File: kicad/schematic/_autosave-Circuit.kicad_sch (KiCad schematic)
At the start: 54 parts, among them M1 Motor_DC, M2 Motor_DC, M3 Motor_DC, M4 Motor_DC, M5 Motor_DC, M6 Motor_DC, M7 Motor_DC, M8 Motor_DC, Q1 AO3400A, Q2 AO3400A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

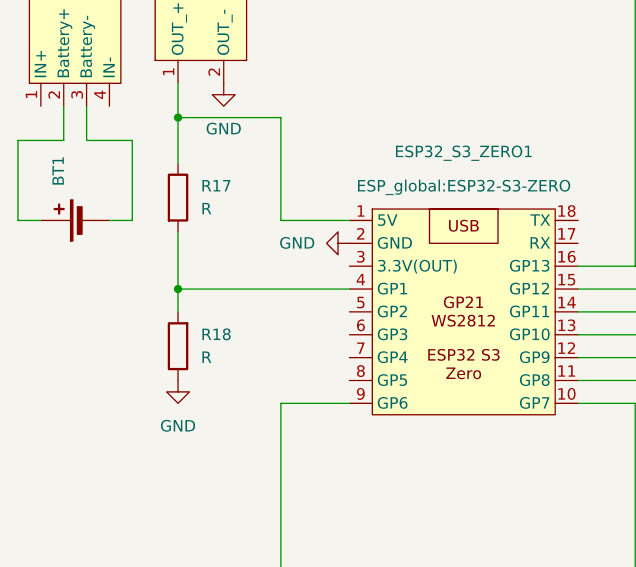
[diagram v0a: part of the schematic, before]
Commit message: added prototype PCB design. Missing: Connection to Pads, Border, Size
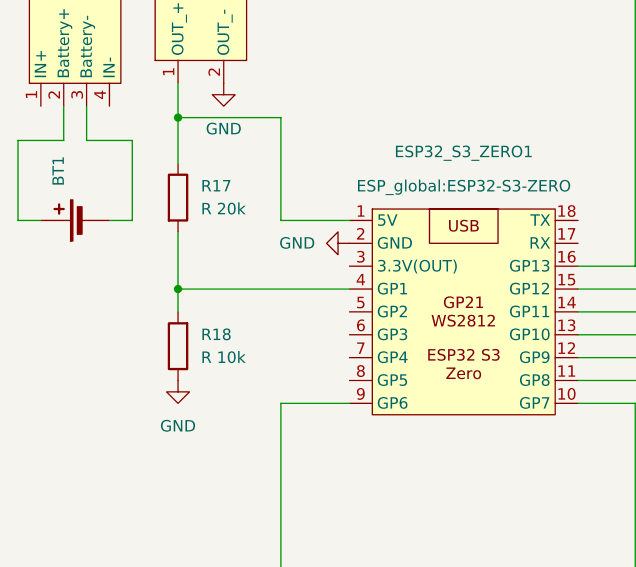
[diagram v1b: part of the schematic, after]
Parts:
- R17: value R -> R 20k
- R18: value R -> R 10k
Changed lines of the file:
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@@
 			)
 		)
-		(property "Value" "R"
+		(property "Value" "R 10k"
 			(at 161.29 114.2999 0)
 			(effects
@@
 			)
 		)
-		(property "Value" "R"
+		(property "Value" "R 20k"
 			(at 161.29 97.7899 0)
 			(effects
